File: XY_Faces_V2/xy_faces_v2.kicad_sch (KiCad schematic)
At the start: 25 parts, among them J1 CON-5040500591, J2 Conn_01x01, J3 Conn_01x01, J4 Conn_01x01, J5 Conn_01x01, U1 VEML7700, U2 MCP9808_DFN, U3 DRV2605LDGS

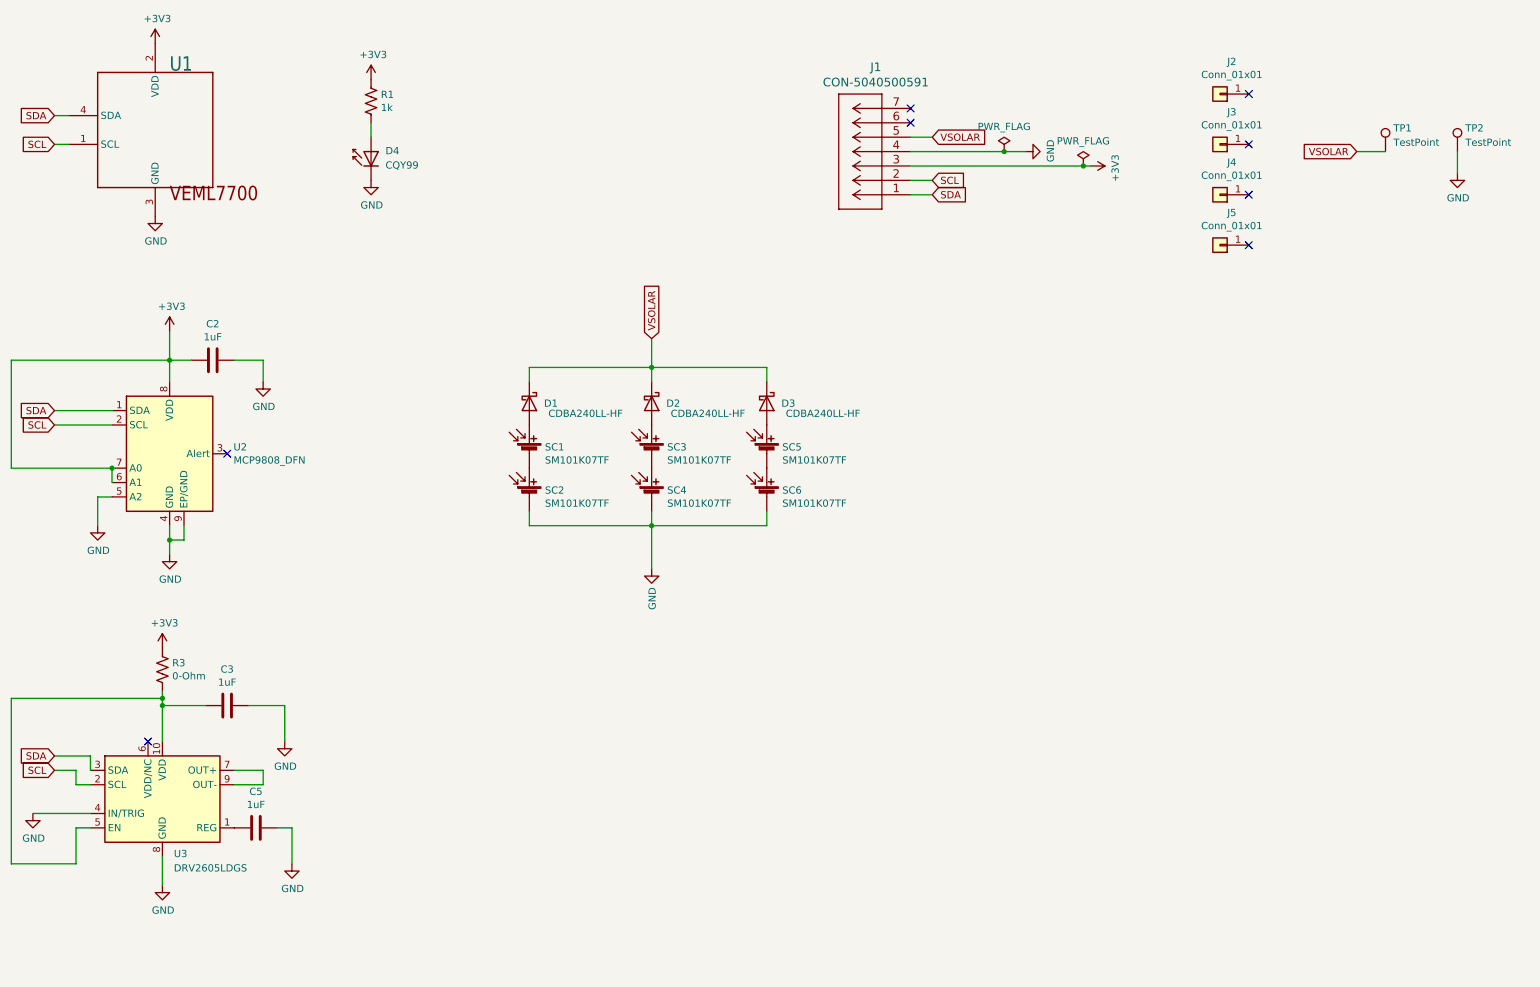
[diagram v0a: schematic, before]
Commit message: Changed Connector Scheme for V2 XY Solar
Changed schematic to a 6pos connector for the picolocks and a 12-pos connector for board to board action
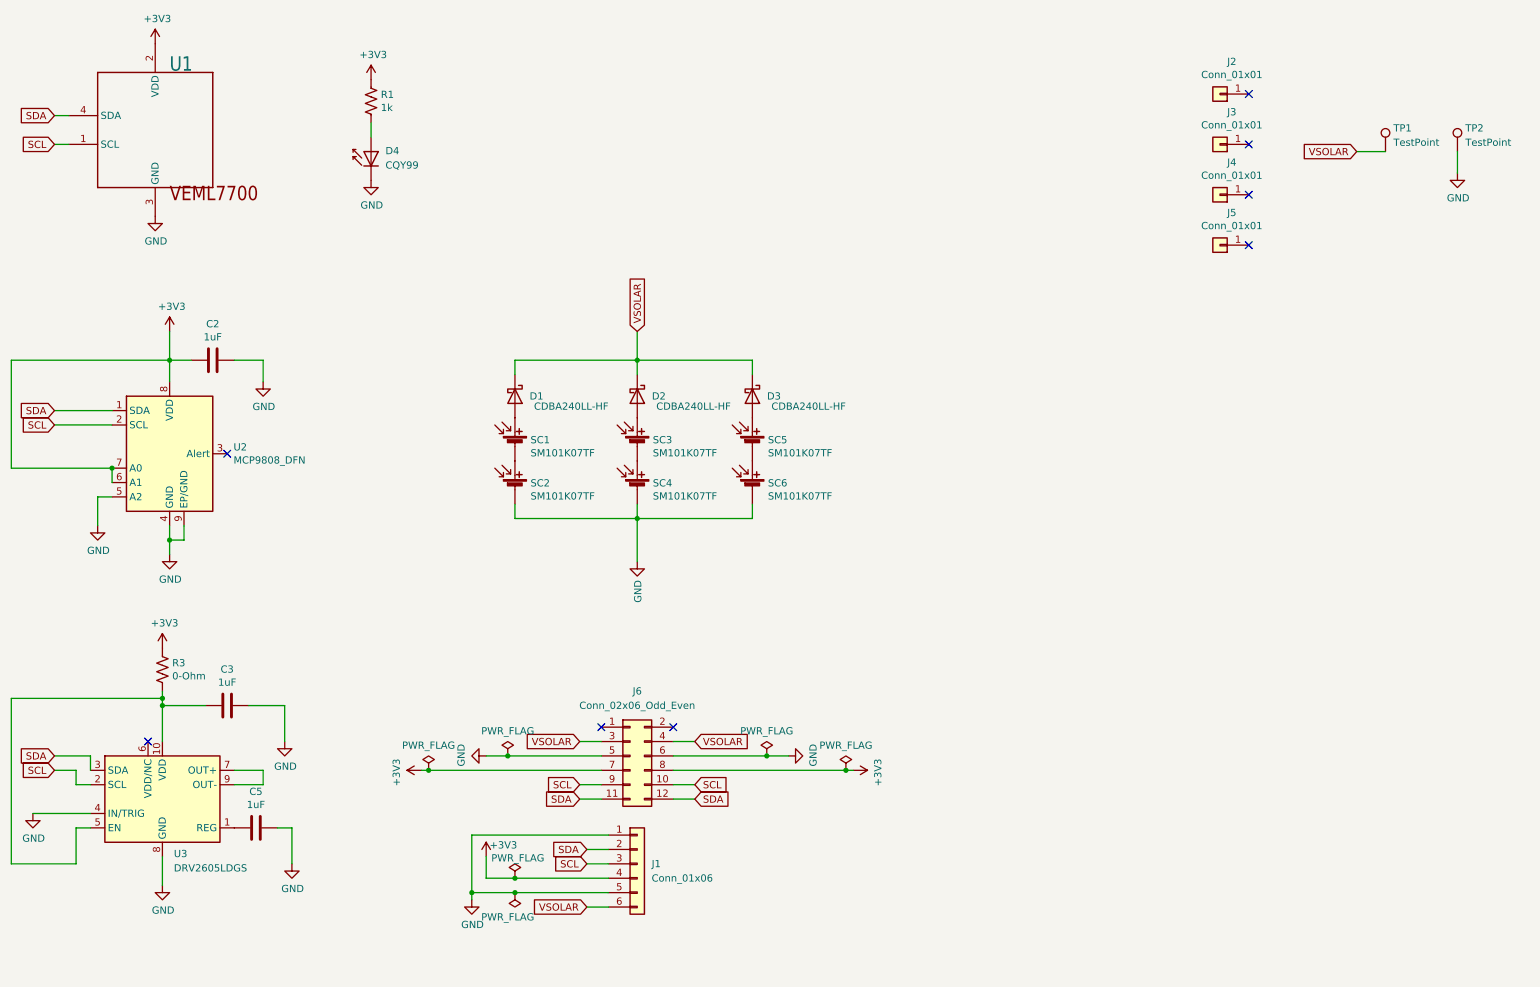
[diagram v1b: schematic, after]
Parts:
- removed J1: CON-5040500591, SolarPanelBoards:CON_5040500591, symbol solar-panel-NoCutout-rescue:CON-5040500591-ExtraComponents
- added J1: Conn_01x06, symbol Connector_Generic:Conn_01x06
- added J6: Conn_02x06_Odd_Even, Connector_Hirose:Hirose_DF11-12DP-2DSA_2x06_P2.00mm_Vertical, symbol Connector_Generic:Conn_02x06_Odd_Even
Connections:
- net +3V3: now also J1.4 (Pin_4), J6.7 (Pin_7), J6.8 (Pin_8)
- net GND: now also J1.1 (Pin_1), J1.5 (Pin_5), J6.5 (Pin_5), J6.6 (Pin_6)
- net SCL: now also J1.3 (Pin_3), J6.10 (Pin_10), J6.9 (Pin_9)
- net SDA: now also J1.2 (Pin_2), J6.11 (Pin_11), J6.12 (Pin_12)
- net VSOLAR: now also J1.6 (Pin_6), J6.3 (Pin_3), J6.4 (Pin_4)
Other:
- moved on the sheet: D1, D2, D3, SC1, SC2, SC3, SC4, SC5, SC6

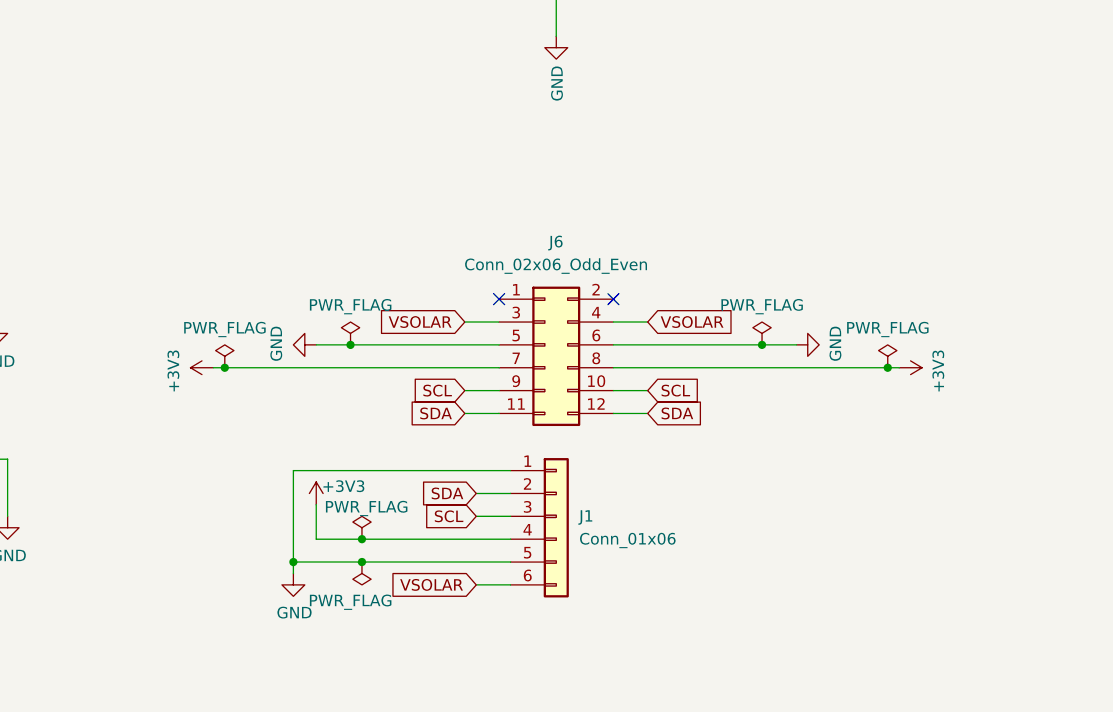
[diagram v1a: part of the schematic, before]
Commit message: Updated Boards with DF13 Connectors
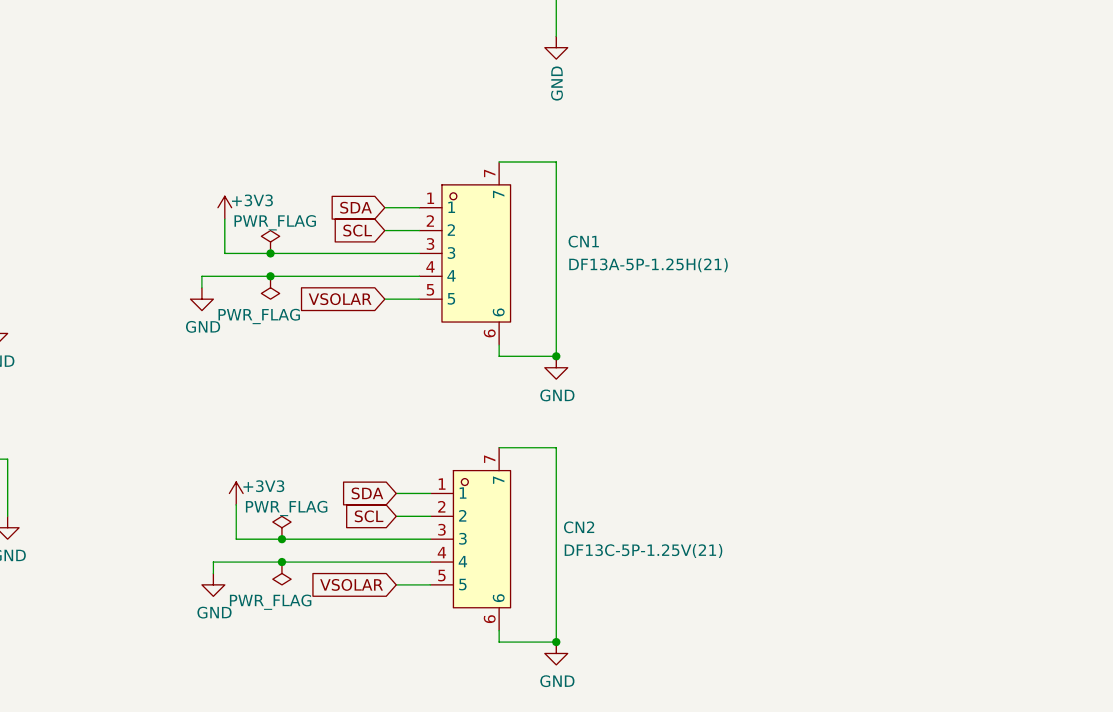
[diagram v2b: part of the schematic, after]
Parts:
- removed J1: Conn_01x06, symbol Connector_Generic:Conn_01x06
- removed J6: Conn_02x06_Odd_Even, Connector_Hirose:Hirose_DF11-12DP-2DSA_2x06_P2.00mm_Vertical, symbol Connector_Generic:Conn_02x06_Odd_Even
- added CN1: DF13A-5P-1.25H(21), easyeda2kicad:CONN-SMD_5P-P1.25_HRS_DF13A-5P-1.25H, symbol easyeda2kicad:DF13A-5P-1.25H(21)
- added CN2: DF13C-5P-1.25V(21), easyeda2kicad:CONN-SMD_DF13C-5P-1.25V-21, symbol easyeda2kicad:DF13C-5P-1.25V(21)
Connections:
- net +3V3: now also CN1.3, CN2.3
- net GND: now also CN1.4, CN1.6, CN1.7, CN2.4, CN2.6, CN2.7
- net SCL: now also CN1.2, CN2.2
- net SDA: now also CN1.1, CN2.1
- net VSOLAR: now also CN1.5, CN2.5
- no-connect marks 8 -> 6
